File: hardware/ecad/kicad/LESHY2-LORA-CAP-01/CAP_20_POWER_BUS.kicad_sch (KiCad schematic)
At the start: 0 parts

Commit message: complete H2.4.2 LoRa Cap root
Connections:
- no-connect marks 0 -> 5
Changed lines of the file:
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@@
 	(generator_version "10.0")
 	(paper "A4")
+	(hierarchical_label "5V_IN"
+		(shape bidirectional)
+		(at 20.32 20.32 0)
+		(effects (font (size 1.27 1.27)))
+	)
+	(wire
+		(pts (xy 20.32 20.32) (xy 25.40 20.32))
+		(stroke (width 0) (type default))
+	)
+	(no_connect (at 25.40 20.32)
+	)
+	(hierarchical_label "GND"
+		(shape bidirectional)
+		(at 20.32 25.40 0)
+		(effects (font (size 1.27 1.27)))
+	)
+	(wire
+		(pts (xy 20.32 25.40) (xy 25.40 25.40))
+		(stroke (width 0) (type default))
+	)
+	(no_connect (at 25.40 25.40)
+	)
+	(hierarchical_label "CAP_3V3"
+		(shape bidirectional)
+		(at 20.32 30.48 0)
+		(effects (font (size 1.27 1.27)))
+	)
+	(wire
+		(pts (xy 20.32 30.48) (xy 25.40 30.48))
+		(stroke (width 0) (type default))
+	)
+	(no_connect (at 25.40 30.48)
+	)
+	(hierarchical_label "IDENTITY_SCL"
+		(shape bidirectional)
+		(at 190.50 20.32 180)
+		(effects (font (size 1.27 1.27)) (justify right))
+	)
+	(wire
+		(pts (xy 190.50 20.32) (xy 185.42 20.32))
+		(stroke (width 0) (type default))
+	)
+	(no_connect (at 185.42 20.32)
+	)
+	(hierarchical_label "IDENTITY_SDA"
+		(shape bidirectional)
+		(at 190.50 25.40 180)
+		(effects (font (size 1.27 1.27)) (justify right))
+	)
+	(wire
+		(pts (xy 190.50 25.40) (xy 185.42 25.40))
+		(stroke (width 0) (type default))
+	)
+	(no_connect (at 185.42 25.40)
+	)
 	(sheet_instances
 		(path "/"

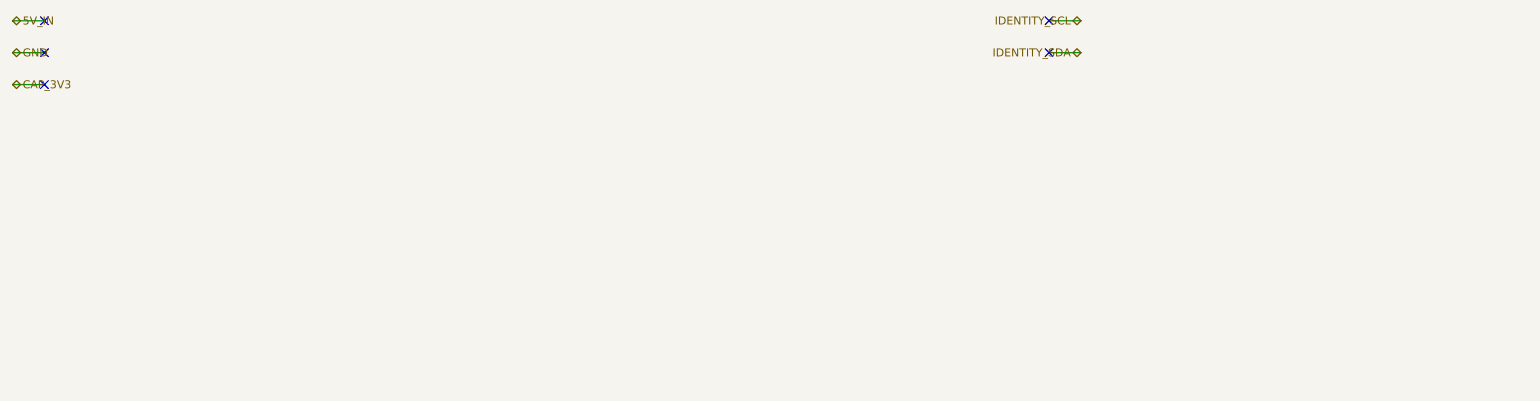
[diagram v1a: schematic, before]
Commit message: complete H2.4.4 LoRa power and identity
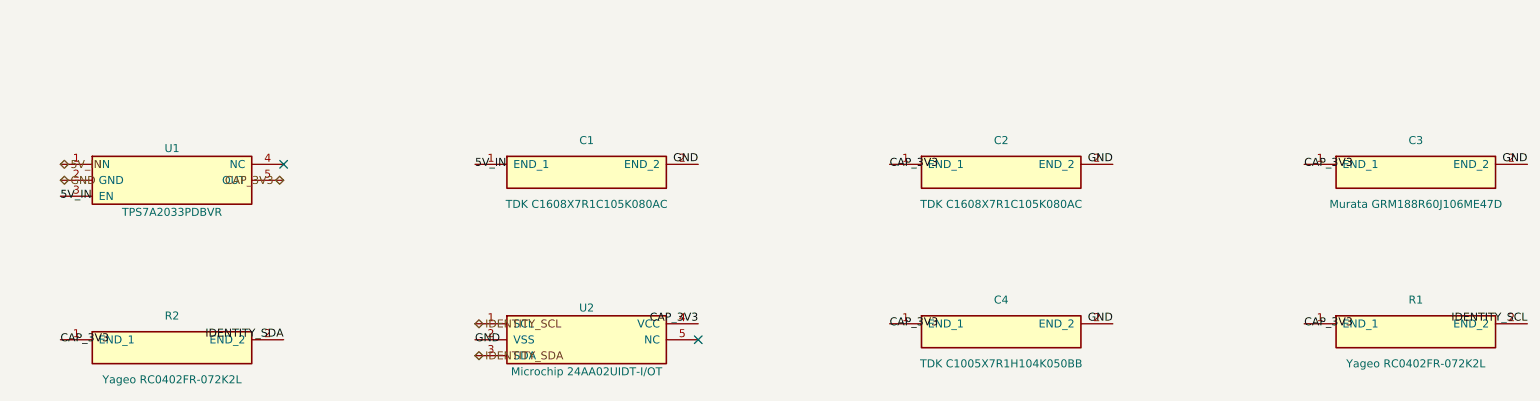
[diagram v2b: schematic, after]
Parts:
- added C1: TDK C1608X7R1C105K080AC, Capacitor_SMD:C_0603_1608Metric, symbol Leshy2:CAP20_LOCAL_REGULATOR_INPUT
- added C2: TDK C1608X7R1C105K080AC, Capacitor_SMD:C_0603_1608Metric, symbol Leshy2:CAP20_LOCAL_REGULATOR_OUTPUT
- added C3: Murata GRM188R60J106ME47D, Capacitor_SMD:C_0603_1608Metric, symbol Leshy2:CAP20_RADIO_BULK
- added C4: TDK C1005X7R1H104K050BB, Capacitor_SMD:C_0402_1005Metric, symbol Leshy2:CAP20_IDENTITY_BYPASS
- added R1: Yageo RC0402FR-072K2L, Resistor_SMD:R_0402_1005Metric, symbol Leshy2:CAP20_IDENTITY_SCL_PULLUP
- added R2: Yageo RC0402FR-072K2L, Resistor_SMD:R_0402_1005Metric, symbol Leshy2:CAP20_IDENTITY_SDA_PULLUP
- added U1: TPS7A2033PDBVR, Package_TO_SOT_SMD:SOT-23-5, symbol Leshy2:CAP20_LOCAL_REGULATOR
- added U2: Microchip 24AA02UIDT-I/OT, Package_TO_SOT_SMD:SOT-23-5, symbol Leshy2:CAP20_IDENTITY
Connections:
- net 5V_IN: now also C1.1 (END_1), U1.1 (IN), U1.3 (EN)
- net CAP_3V3: now also C2.1 (END_1), C3.1 (END_1), C4.1 (END_1), R1.1 (END_1), R2.1 (END_1), U1.5 (OUT), U2.4 (VCC)
- net GND: now also C1.2 (END_2), C2.2 (END_2), C3.2 (END_2), C4.2 (END_2), U1.2 (GND), U2.2 (VSS)
- net IDENTITY_SCL: now also R1.2 (END_2), U2.1 (SCL)
- net IDENTITY_SDA: now also R2.2 (END_2), U2.3 (SDA)
- no-connect marks 5 -> 2
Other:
- title: (none) -> Leshy2 LoRa Cap — 5-V to low-noise 3.3-V power and identity

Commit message: complete H2 schematic review package
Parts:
- renumbered C1 to C20001, C2 to C20002, C3 to C20003, C4 to C20004, R1 to R20001, R2 to R20002, U1 to U20001, U2 to U20002
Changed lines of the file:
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@@
 		(on_board yes)
 		(dnp no)
-		(property "Reference" "U1"
+		(property "Reference" "U20001"
 			(at 45.72 40.64 0)
 			(show_name no)
@@
 			(project "LESHY2-LORA-CAP-01"
 				(path "/ce195de2-40c3-53e9-9426-2f8dd4988e06"
-					(reference "U1")
+					(reference "U20001")
 					(unit 1)
 				)
@@
 		(on_board yes)
 		(dnp no)
-		(property "Reference" "C1"
+		(property "Reference" "C20001"
 			(at 111.76 39.37 0)
 			(show_name no)
@@
 			(project "LESHY2-LORA-CAP-01"
 				(path "/ce195de2-40c3-53e9-9426-2f8dd4988e06"
-					(reference "C1")
+					(reference "C20001")
 					(unit 1)
 				)
@@
 		(on_board yes)
 		(dnp no)
-		(property "Reference" "C2"
+		(property "Reference" "C20002"
 			(at 177.80 39.37 0)
 			(show_name no)
@@
 			(project "LESHY2-LORA-CAP-01"
 				(path "/ce195de2-40c3-53e9-9426-2f8dd4988e06"
-					(reference "C2")
+					(reference "C20002")
 					(unit 1)
 				)
@@
 		(on_board yes)
 		(dnp no)
-		(property "Reference" "C3"
+		(property "Reference" "C20003"
 			(at 243.84 39.37 0)
 			(show_name no)
@@
 			(project "LESHY2-LORA-CAP-01"
 				(path "/ce195de2-40c3-53e9-9426-2f8dd4988e06"
-					(reference "C3")
+					(reference "C20003")
 					(unit 1)
 				)
@@
 		(on_board yes)
 		(dnp no)
-		(property "Reference" "U2"
+		(property "Reference" "U20002"
 			(at 111.76 66.04 0)
 			(show_name no)
@@
 			(project "LESHY2-LORA-CAP-01"
 				(path "/ce195de2-40c3-53e9-9426-2f8dd4988e06"
-					(reference "U2")
+					(reference "U20002")
 					(unit 1)
 				)
@@
 		(on_board yes)
 		(dnp no)
-		(property "Reference" "C4"
+		(property "Reference" "C20004"
 			(at 177.80 64.77 0)
 			(show_name no)
@@
 			(project "LESHY2-LORA-CAP-01"
 				(path "/ce195de2-40c3-53e9-9426-2f8dd4988e06"
-					(reference "C4")
+					(reference "C20004")
 					(unit 1)
 				)
@@
 		(on_board yes)
 		(dnp no)
-		(property "Reference" "R1"
+		(property "Reference" "R20001"
 			(at 243.84 64.77 0)
 			(show_name no)
@@
 			(project "LESHY2-LORA-CAP-01"
 				(path "/ce195de2-40c3-53e9-9426-2f8dd4988e06"
-					(reference "R1")
+					(reference "R20001")
 					(unit 1)
 				)
@@
 		(on_board yes)
 		(dnp no)
-		(property "Reference" "R2"
+		(property "Reference" "R20002"
 			(at 45.72 67.31 0)
 			(show_name no)
@@
 			(project "LESHY2-LORA-CAP-01"
 				(path "/ce195de2-40c3-53e9-9426-2f8dd4988e06"
-					(reference "R2")
-					(unit 1)
-				)
+					(reference "R20002")
+					(unit 1)
+				)

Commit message: Optimize H1 display and stocked BOM routes
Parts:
- C20004: value TDK C1005X7R1H104K050BB -> Yageo CC0402KRX7R9BB104
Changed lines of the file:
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@@
 			(effects (font (size 1.27 1.27)))
 		)
-		(property "Value" "TDK C1005X7R1H104K050BB"
+		(property "Value" "Yageo CC0402KRX7R9BB104"
 			(at 177.80 74.93 0)
 			(show_name no)

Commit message: Replace six pre-order resistor identities
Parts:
- R20001, R20002: value Yageo RC0402FR-072K2L -> UNI-ROYAL 0402WGF2201TCE
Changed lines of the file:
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@@
 			(effects (font (size 1.27 1.27)))
 		)
-		(property "Value" "Yageo RC0402FR-072K2L"
+		(property "Value" "UNI-ROYAL 0402WGF2201TCE"
 			(at 243.84 74.93 0)
 			(show_name no)
@@
 			(effects (font (size 1.27 1.27)))
 		)
-		(property "Value" "Yageo RC0402FR-072K2L"
+		(property "Value" "UNI-ROYAL 0402WGF2201TCE"
 			(at 45.72 77.47 0)
 			(show_name no)
